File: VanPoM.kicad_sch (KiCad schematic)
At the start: 153 parts, among them IC1 TLV70433DBVT, IC2 UCC27517DBVR, IC3 SN74LV4052APWR, J1 Conn_03x26_Row_Letter_First, J10 UART3, J11 UART4, J2 OSTT7020150, J3 OSTT7020150, J4 OSTT7020150, J5 OSTT7020150, J6 OSTT7020150, J7 UART1, J8 UART1, J9 UART2, Q1 CSD18540Q5B, Q10 CSD18540Q5B, Q11 CSD18540Q5B, Q2 NX7002AK,215, Q3 BSS84W-7-F, Q4 CSD19531Q5A, Q5 CSD19531Q5A, Q6 CSD19531Q5A, Q7 CSD19531Q5A, Q8 CSD18540Q5B, Q9 CSD18540Q5B, U1 BQ34Z100-R2, U10 LM5009MM, U11 ESP32-S3-DEVKITC-1-N8R2, U12 TLA2528IRTER, U13 TVS3300DRV, U14 TVS3300DRV, U15 TVS3300DRV, U16 TVS3300DRV, U17 TVS3300DRV, U2 LM5109BMA/NOPB, U3 LM5109BMA/NOPB, U4 INA240A2D, U5 INA240A2D, U6 INA240A2D, U7 LM74700, U8 LM74700, U9 LM74700

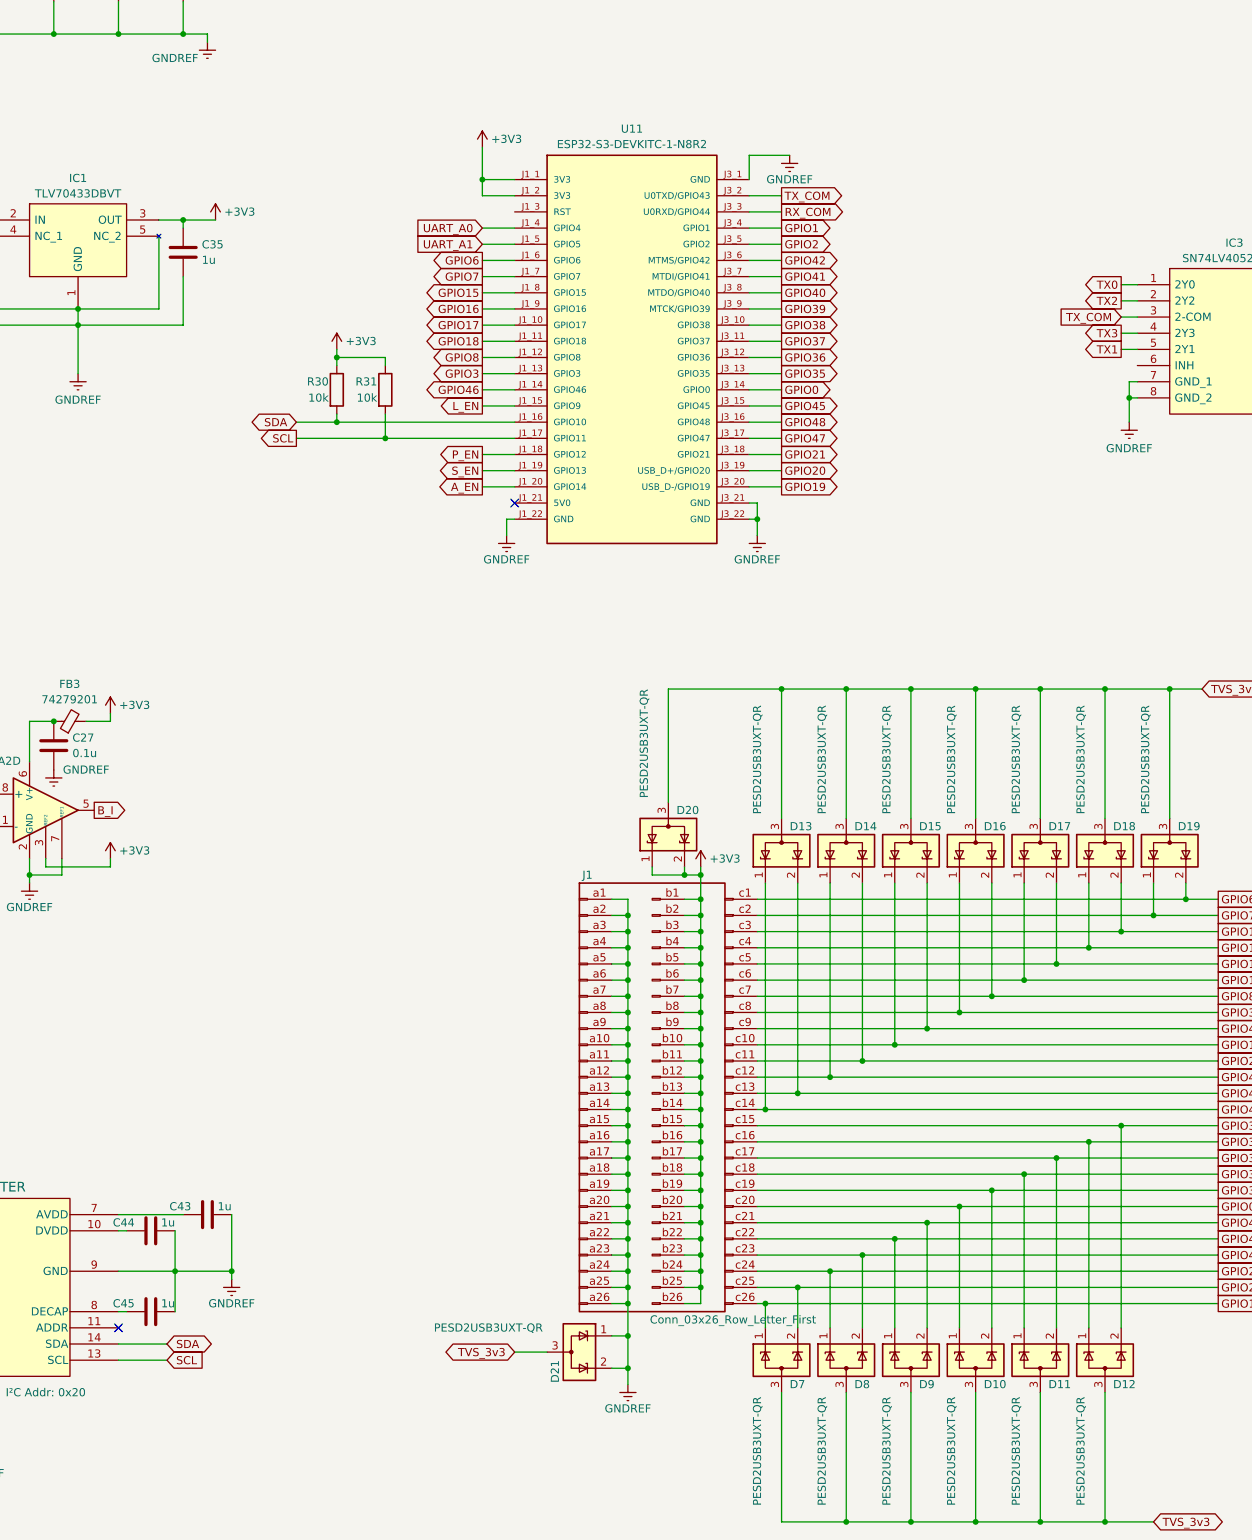
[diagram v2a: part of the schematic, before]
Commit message: + UART pull-ups
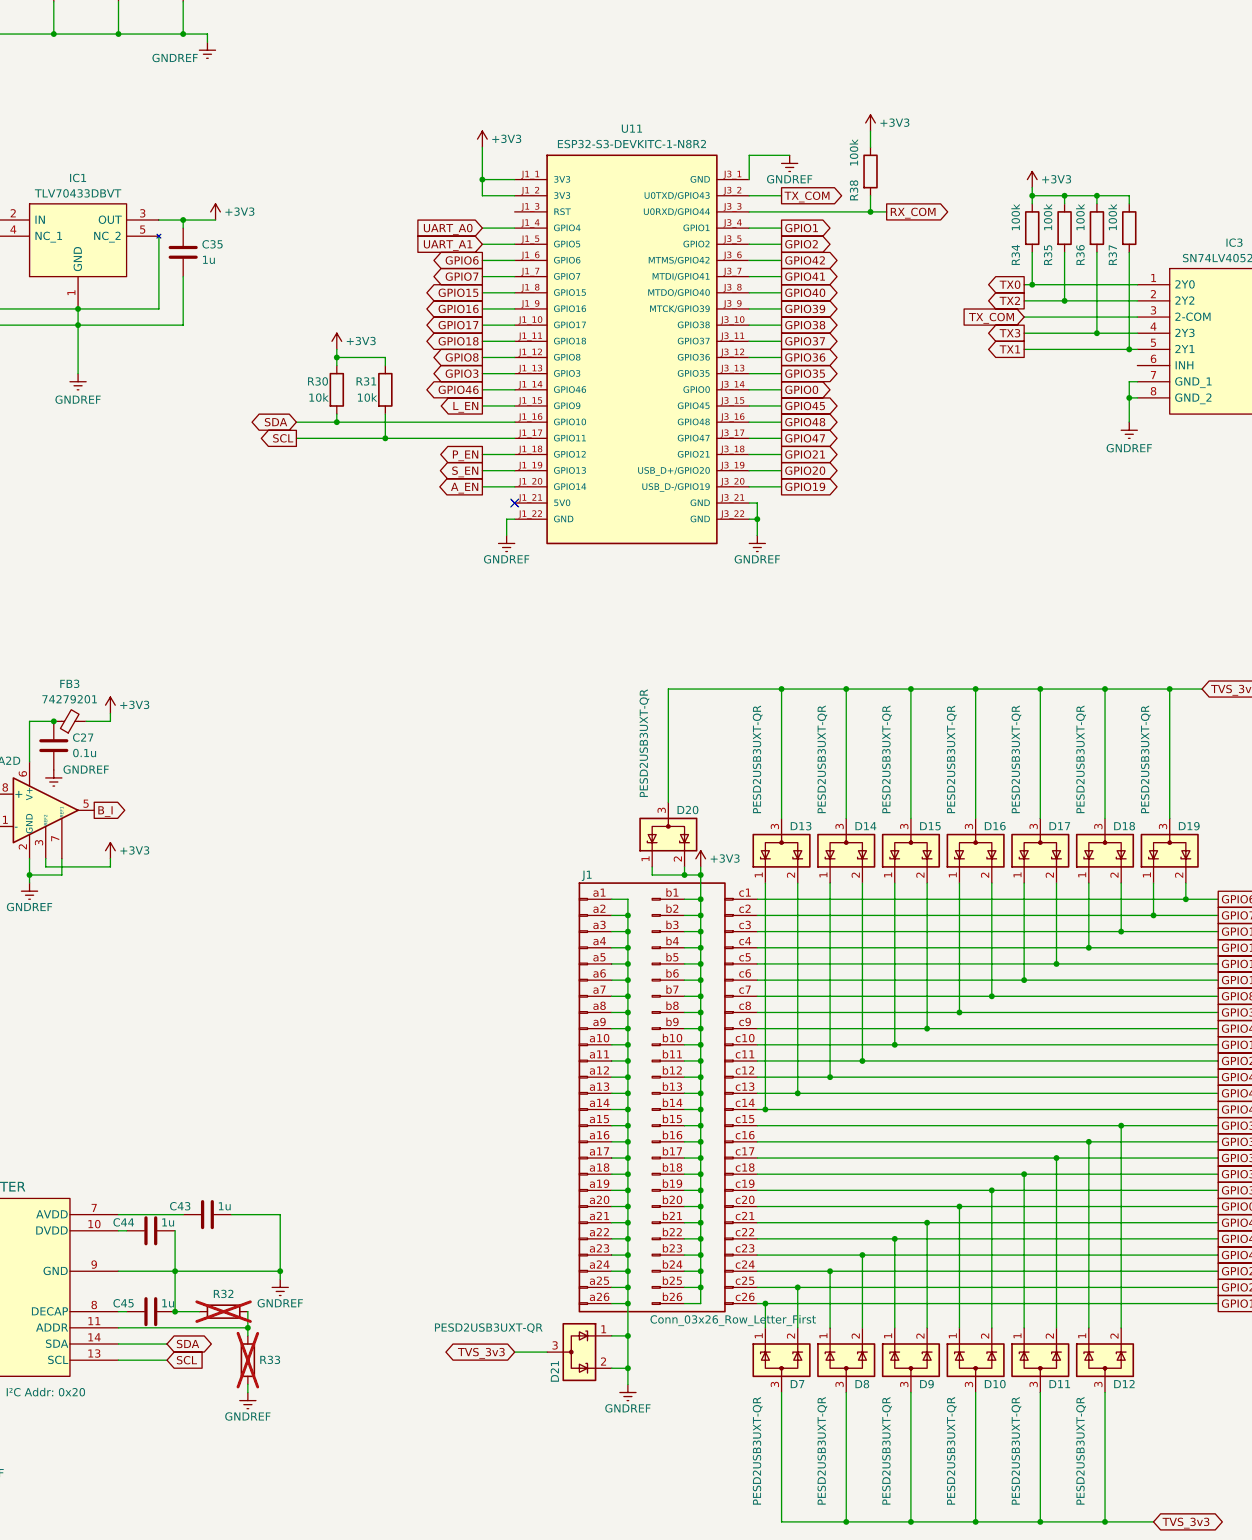
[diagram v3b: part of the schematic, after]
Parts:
- added R32, R33: R, symbol Device:R
- added R34, R35, R36, R37, R38: 100k, symbol Device:R
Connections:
- net +3V3: now also R34.1, R35.1, R36.1, R37.1, R38.1
- net GNDREF: now also R32.1, R33.1
- net RX_COM: now also R38.2
- net TX0: now also R34.2
- net TX1: now also R37.2
- net TX2: now also R35.2
- net TX3: now also R36.2
- net at U12.11 (ADDR): now also R32.2, R33.2
- no-connect marks 2 -> 1

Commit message: +++ PCB; f many small things
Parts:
- removed C30: 10u, symbol Perso:Cv
- removed C31: 1u, symbol Perso:Cv
- removed C32: 0.022u, symbol Perso:Cv
- removed C33: 10n, symbol Device:C
- removed D15, D16, D21: PESD2USB3UXT-QR, Package_TO_SOT_SMD:SOT-23, symbol Perso:PESD2USB3UXT-QR
- removed D6: B1100B-13-F, symbol Device:D_Schottky
- removed J1: Conn_03x26_Row_Letter_First, Perso:PinHeader_3x25_P2.54mm_Vertical, symbol Perso:Conn_03x26_Row_Letter_First
- removed J3: OSTT7020150, Perso:CONN2_OSTT7020150_OST, symbol Perso:OSTT7020150
- removed R21: 3.00, symbol Device:R
- removed R22, R23: 1.8M, symbol Device:R
- removed U10: LM5009MM, Package_SO:MSOP-8_3x3mm_P0.65mm, symbol Regulator_Switching:LM5009MM
- added C27: 10u, Capacitor_SMD:C_1210_3225Metric_Pad1.33x2.70mm_HandSolder, symbol Perso:Cv
- added C28: 0.022u, Capacitor_SMD:C_1206_3216Metric_Pad1.33x1.80mm_HandSolder, symbol Perso:Cv
- added C29: 50n, Capacitor_SMD:C_0402_1005Metric_Pad0.74x0.62mm_HandSolder, symbol Device:C
- added C30: 10n, Capacitor_SMD:C_0402_1005Metric_Pad0.74x0.62mm_HandSolder, symbol Device:C
- added C43: 0.1u, Capacitor_SMD:C_0603_1608Metric_Pad1.08x0.95mm_HandSolder, symbol Device:C
- added D6: PESD2USB3UXT-QR, Package_TO_SOT_SMD:SOT-23-3, symbol Perso:PESD2USB3UXT-QR
- added J5: OSTT7020150, TerminalBlock_MetzConnect:TerminalBlock_MetzConnect_Type073_RT02602HBLU_1x02_P5.08mm_Horizontal, symbol Perso:OSTT7020150
- added J6: Conn_03x23_Row_Letter_First, Perso:PinHeader_3x23_P2.54mm_Vertical, symbol Perso:Conn_03x23_Row_Letter_First
- added R30, R31: 200k, Resistor_SMD:R_0805_2012Metric_Pad1.20x1.40mm_HandSolder, symbol Device:R
- added U10: LM5163DDAR, Perso:SOIC-8-1EP_3.9x4.9mm_P1.27mm_EP2.34x2.34mm_ThermalVias, symbol Perso:LM5163DDAR
- added U18: TVS3300DRV, Package_SON:WSON-6-1EP_2x2mm_P0.65mm_EP1x1.6mm, symbol Perso:TVS3300DRV
- C1: renamed from C7; footprint (none) -> Capacitor_SMD:C_0603_1608Metric_Pad1.08x0.95mm_HandSolder; Manufacturer_Part_Number (none) -> GRM188R72A102KA01J; Price (none) -> 0.3
- C10: renamed from C8; footprint (none) -> Capacitor_SMD:C_0603_1608Metric_Pad1.08x0.95mm_HandSolder; Manufacturer_Part_Number (none) -> GRM188R72A102KA01J; Price (none) -> 0.3
- C11: renamed from C21; footprint (none) -> Capacitor_SMD:C_1210_3225Metric_Pad1.33x2.70mm_HandSolder; Manufacturer_Part_Number (none) -> GRM32EC72A106KE05K; Price (none) -> 0.83
- C12: renamed from C22; footprint (none) -> Capacitor_SMD:C_1210_3225Metric_Pad1.33x2.70mm_HandSolder; Manufacturer_Part_Number (none) -> GRM32EC72A106KE05K; Price (none) -> 0.83
- C13: renamed from C23; footprint (none) -> Capacitor_THT:CP_Radial_D16.0mm_P7.50mm; Manufacturer_Part_Number (none) -> EKYB800ELL102MLP1S; Price (none) -> 1.50
- C14: renamed from C1; footprint (none) -> Capacitor_SMD:C_0603_1608Metric_Pad1.08x0.95mm_HandSolder; Manufacturer_Part_Number (none) -> KGM15BR71H104JT; Price (none) -> 0.09
- C15: renamed from C2; value 1 -> 1u; footprint (none) -> Capacitor_SMD:C_0402_1005Metric_Pad0.74x0.62mm_HandSolder; Manufacturer_Part_Number (none) -> GRM155C81A105KA12D; Price (none) -> 0.09
- C16: renamed from C24; footprint (none) -> Capacitor_SMD:C_0603_1608Metric_Pad1.08x0.95mm_HandSolder; Manufacturer_Part_Number (none) -> KGM15BR71H104JT; Price (none) -> 0.09
- C17: renamed from C20; value 47u -> 0.1u; footprint (none) -> Capacitor_SMD:C_0603_1608Metric_Pad1.08x0.95mm_HandSolder; Manufacturer_Part_Number (none) -> KGM15BR71H104JT; Price (none) -> 0.09
- C18: renamed from C28; value 47u -> 0.1u; footprint (none) -> Capacitor_SMD:C_0603_1608Metric_Pad1.08x0.95mm_HandSolder; Manufacturer_Part_Number (none) -> KGM15BR71H104JT; Price (none) -> 0.09
- C19: renamed from C14; footprint (none) -> Capacitor_THT:CP_Radial_D18.0mm_P7.50mm; Manufacturer_Part_Number (none) -> EKY-800ELL122MM40S; Price (none) -> 1.83
- C2: renamed from C3; footprint (none) -> Capacitor_SMD:C_0805_2012Metric_Pad1.18x1.45mm_HandSolder; Manufacturer_Part_Number (none) -> KGM21AR71E105JU; Price (none) -> 0.3
- C20: renamed from C15; footprint (none) -> Capacitor_THT:CP_Radial_D18.0mm_P7.50mm; Manufacturer_Part_Number (none) -> EKY-800ELL122MM40S; Price (none) -> 1.83
- C21: renamed from C29; value 47u -> 0.1u; footprint (none) -> Capacitor_SMD:C_0603_1608Metric_Pad1.08x0.95mm_HandSolder; Manufacturer_Part_Number (none) -> KGM15BR71H104JT; Price (none) -> 0.09
- C22: renamed from C13; footprint (none) -> Capacitor_SMD:C_1206_3216Metric_Pad1.33x1.80mm_HandSolder; Manufacturer_Part_Number (none) -> GRM31CC72A475KE11L; Price (none) -> 0.6
- C23: renamed from C16; footprint (none) -> Capacitor_SMD:C_1206_3216Metric_Pad1.33x1.80mm_HandSolder; Manufacturer_Part_Number (none) -> GRM31CC72A475KE11L; Price (none) -> 0.6
- C24: renamed from C17; footprint (none) -> Capacitor_SMD:C_1206_3216Metric_Pad1.33x1.80mm_HandSolder; Manufacturer_Part_Number (none) -> GRM31CC72A475KE11L; Price (none) -> 0.6
- C25: renamed from C18; footprint (none) -> Capacitor_SMD:C_1206_3216Metric_Pad1.33x1.80mm_HandSolder; Manufacturer_Part_Number (none) -> GRM31CC72A475KE11L; Price (none) -> 0.6
- C26: renamed from C19; footprint (none) -> Capacitor_SMD:C_1206_3216Metric_Pad1.33x1.80mm_HandSolder; Manufacturer_Part_Number (none) -> GRM31CC72A475KE11L; Price (none) -> 0.6
- C3: renamed from C4; footprint (none) -> Capacitor_SMD:C_0603_1608Metric_Pad1.08x0.95mm_HandSolder; Manufacturer_Part_Number (none) -> 885012206004; Price (none) -> 0.05
- C31: renamed from C34; footprint (none) -> Capacitor_SMD:C_0805_2012Metric_Pad1.18x1.45mm_HandSolder; Manufacturer_Part_Number (none) -> KGM21AR71E105JU; Price (none) -> 0.3; Voltage (none) -> 25V
- C32: renamed from C35; footprint (none) -> Capacitor_SMD:C_0402_1005Metric_Pad0.74x0.62mm_HandSolder; Manufacturer_Part_Number (none) -> GRM155C81A105KA12D; Price (none) -> 0.09
- C33: renamed from C25; footprint (none) -> Capacitor_SMD:C_0603_1608Metric_Pad1.08x0.95mm_HandSolder; Manufacturer_Part_Number (none) -> KGM15BR71H104JT; Price (none) -> 0.09
- C34: renamed from C26; footprint (none) -> Capacitor_SMD:C_0603_1608Metric_Pad1.08x0.95mm_HandSolder; Manufacturer_Part_Number (none) -> KGM15BR71H104JT; Price (none) -> 0.09
- C35: renamed from C27; footprint (none) -> Capacitor_SMD:C_0603_1608Metric_Pad1.08x0.95mm_HandSolder; Manufacturer_Part_Number (none) -> KGM15BR71H104JT; Price (none) -> 0.09
- C36, C37, C38, C39, C40, C41, C42: footprint (none) -> Capacitor_SMD:C_0603_1608Metric_Pad1.08x0.95mm_HandSolder; Manufacturer_Part_Number (none) -> KGM15BR71H104JT; Price (none) -> 0.09
- C4: renamed from C5; footprint (none) -> Capacitor_SMD:C_0402_1005Metric_Pad0.74x0.62mm_HandSolder; Manufacturer_Part_Number (none) -> UMK105B7561KV-F; Price (none) -> 0.09
- C44, C45: footprint (none) -> Capacitor_SMD:C_0402_1005Metric_Pad0.74x0.62mm_HandSolder; Manufacturer_Part_Number (none) -> GRM155C81A105KA12D; Price (none) -> 0.09
- C46: renamed from C43; footprint (none) -> Capacitor_SMD:C_0402_1005Metric_Pad0.74x0.62mm_HandSolder; Manufacturer_Part_Number (none) -> GRM155C81A105KA12D; Price (none) -> 0.09
- C5: renamed from C6; footprint (none) -> Capacitor_SMD:C_0603_1608Metric_Pad1.08x0.95mm_HandSolder; Manufacturer_Part_Number (none) -> KGM15BR71H104JT; Price (none) -> 0.09
- C6: renamed from C12; footprint (none) -> Capacitor_SMD:C_0603_1608Metric_Pad1.08x0.95mm_HandSolder; Manufacturer_Part_Number (none) -> KGM15BR71H104JT; Price (none) -> 0.09
- C7: renamed from C11; footprint (none) -> Capacitor_SMD:C_0402_1005Metric_Pad0.74x0.62mm_HandSolder; Manufacturer_Part_Number (none) -> UMK105B7561KV-F; Price (none) -> 0.09
- C8: renamed from C10; footprint (none) -> Capacitor_SMD:C_0603_1608Metric_Pad1.08x0.95mm_HandSolder; Manufacturer_Part_Number (none) -> 885012206004; Price (none) -> 0.05
- C9: footprint (none) -> Capacitor_SMD:C_0805_2012Metric_Pad1.18x1.45mm_HandSolder; Manufacturer_Part_Number (none) -> KGM21AR71E105JU; Price (none) -> 0.3
- D1: renamed from D3; footprint (none) -> Diode_SMD:D_SMA; Manufacturer_Part_Number (none) -> B1100-13-F; Price (none) -> 0.28
- D10: renamed from D8; footprint Package_TO_SOT_SMD:SOT-23 -> Package_TO_SOT_SMD:SOT-23-3; Manufacturer_Part_Number (none) -> PESD2USB3UXT-QR; Price (none) -> 0.25
- D11: renamed from D14; footprint Package_TO_SOT_SMD:SOT-23 -> Package_TO_SOT_SMD:SOT-23-3; Manufacturer_Part_Number (none) -> PESD2USB3UXT-QR; Price (none) -> 0.25
- D12: renamed from D9; footprint Package_TO_SOT_SMD:SOT-23 -> Package_TO_SOT_SMD:SOT-23-3; Manufacturer_Part_Number (none) -> PESD2USB3UXT-QR; Price (none) -> 0.25
- D13: renamed from D17; footprint Package_TO_SOT_SMD:SOT-23 -> Package_TO_SOT_SMD:SOT-23-3; Manufacturer_Part_Number (none) -> PESD2USB3UXT-QR; Price (none) -> 0.25
- D14: renamed from D10; footprint Package_TO_SOT_SMD:SOT-23 -> Package_TO_SOT_SMD:SOT-23-3; Manufacturer_Part_Number (none) -> PESD2USB3UXT-QR; Price (none) -> 0.25
- D15: renamed from D18; footprint Package_TO_SOT_SMD:SOT-23 -> Package_TO_SOT_SMD:SOT-23-3; Manufacturer_Part_Number (none) -> PESD2USB3UXT-QR; Price (none) -> 0.25
- D16: renamed from D11; footprint Package_TO_SOT_SMD:SOT-23 -> Package_TO_SOT_SMD:SOT-23-3; Manufacturer_Part_Number (none) -> PESD2USB3UXT-QR; Price (none) -> 0.25
- D17: renamed from D19; footprint Package_TO_SOT_SMD:SOT-23 -> Package_TO_SOT_SMD:SOT-23-3; Manufacturer_Part_Number (none) -> PESD2USB3UXT-QR; Price (none) -> 0.25
- D18: renamed from D12; footprint Package_TO_SOT_SMD:SOT-23 -> Package_TO_SOT_SMD:SOT-23-3; Manufacturer_Part_Number (none) -> PESD2USB3UXT-QR; Price (none) -> 0.25
- D2: footprint (none) -> Diode_SMD:D_SMA; Manufacturer_Part_Number (none) -> MURA110T3G; Price (none) -> 0.46
- D21: renamed from D25; footprint Package_TO_SOT_SMD:SOT-23 -> Package_TO_SOT_SMD:SOT-23-3; Manufacturer_Part_Number (none) -> PESD2USB3UXT-QR; Price (none) -> 0.25
- D22: renamed from D24; footprint Package_TO_SOT_SMD:SOT-23 -> Package_TO_SOT_SMD:SOT-23-3; Manufacturer_Part_Number (none) -> PESD2USB3UXT-QR; Price (none) -> 0.25
- D23: footprint Package_TO_SOT_SMD:SOT-23 -> Package_TO_SOT_SMD:SOT-23-3; Manufacturer_Part_Number (none) -> PESD2USB3UXT-QR; Price (none) -> 0.25
- D24: renamed from D22; footprint Package_TO_SOT_SMD:SOT-23 -> Package_TO_SOT_SMD:SOT-23-3; Manufacturer_Part_Number (none) -> PESD2USB3UXT-QR; Price (none) -> 0.25
- D25: renamed from D26; footprint Package_TO_SOT_SMD:SOT-23 -> Package_TO_SOT_SMD:SOT-23-3; Manufacturer_Part_Number (none) -> PESD2USB3UXT-QR; Price (none) -> 0.25
- D3: renamed from D5; footprint (none) -> Diode_SMD:D_SMA; Manufacturer_Part_Number (none) -> MURA110T3G; Price (none) -> 0.46
- D4: footprint (none) -> Diode_SMD:D_SMA; Manufacturer_Part_Number (none) -> B1100-13-F; Price (none) -> 0.28
- D5: renamed from D1; footprint (none) -> Diode_SMD:D_SOD-123; Manufacturer_Part_Number (none) -> BZT52C15-7-F; Price (none) -> 0.13
- D7: renamed from D20; footprint Package_TO_SOT_SMD:SOT-23 -> Package_TO_SOT_SMD:SOT-23-3; Manufacturer_Part_Number (none) -> PESD2USB3UXT-QR; Price (none) -> 0.25
- D8: renamed from D7; footprint Package_TO_SOT_SMD:SOT-23 -> Package_TO_SOT_SMD:SOT-23-3; Manufacturer_Part_Number (none) -> PESD2USB3UXT-QR; Price (none) -> 0.25
- D9: renamed from D13; footprint Package_TO_SOT_SMD:SOT-23 -> Package_TO_SOT_SMD:SOT-23-3; Manufacturer_Part_Number (none) -> PESD2USB3UXT-QR; Price (none) -> 0.25
- FB1, FB2, FB3: footprint (none) -> Capacitor_SMD:C_0805_2012Metric_Pad1.18x1.45mm_HandSolder; Manufacturer_Part_Number (none) -> 74279201; Price (none) -> 0.20
- IC1: renamed from IC2; Price (none) -> 0.78
- IC2: renamed from IC1; Price (none) -> 0.78
- IC3: Price (none) -> 0.39
- J1: renamed from J5; footprint Perso:CONN2_OSTT7020150_OST -> TerminalBlock_MetzConnect:TerminalBlock_MetzConnect_Type073_RT02602HBLU_1x02_P5.08mm_Horizontal; Manufacturer_Part_Number (none) -> EM290802; Price (none) -> 1.58
- J10: renamed from J8; footprint (none) -> Connector_PinHeader_2.54mm:PinHeader_1x04_P2.54mm_Vertical; Manufacturer_Part_Number (none) -> G800W304018EU; Price (none) -> 0.10
- J11: renamed from J7; value UART1 -> I2C; footprint (none) -> Connector_PinHeader_2.54mm:PinHeader_1x04_P2.54mm_Vertical; Manufacturer_Part_Number (none) -> G800W304018EU; Price (none) -> 0.10
- J2, J4: footprint Perso:CONN2_OSTT7020150_OST -> TerminalBlock_MetzConnect:TerminalBlock_MetzConnect_Type073_RT02602HBLU_1x02_P5.08mm_Horizontal; Manufacturer_Part_Number (none) -> EM290802; Price (none) -> 1.58
- J3: renamed from J6; footprint Perso:CONN2_OSTT7020150_OST -> TerminalBlock_MetzConnect:TerminalBlock_MetzConnect_Type073_RT02602HBLU_1x02_P5.08mm_Horizontal; Manufacturer_Part_Number (none) -> EM290802; Price (none) -> 1.58
- J7: renamed from J11; footprint (none) -> Connector_PinHeader_2.54mm:PinHeader_1x04_P2.54mm_Vertical; Manufacturer_Part_Number (none) -> G800W304018EU; Price (none) -> 0.10
- J8: renamed from J10; footprint (none) -> Connector_PinHeader_2.54mm:PinHeader_1x04_P2.54mm_Vertical; Manufacturer_Part_Number (none) -> G800W304018EU; Price (none) -> 0.10
- J9: footprint (none) -> Connector_PinHeader_2.54mm:PinHeader_1x04_P2.54mm_Vertical; Manufacturer_Part_Number (none) -> G800W304018EU; Price (none) -> 0.10
- L1, L2: footprint (none) -> Inductor_SMD:L_Wuerth_HCF-2818; Manufacturer_Part_Number (none) -> 7443642200; Price (none) -> 9.27
- L3: footprint (none) -> Perso:INDPM105103X500N; Manufacturer_Part_Number (none) -> DR1050-221-R; Price (none) -> 0.94
- Q1: renamed from Q5; footprint Package_TO_SOT_SMD:TDSON-8-1 -> Package_SON:VSONP-8-1EP_5x6_P1.27mm; symbol Transistor_FET:CSD19531Q5A -> Perso:CSD19531Q5A; Manufacturer_Part_Number (none) -> CSD19531Q5A; Price (none) -> 1.58
- Q10, Q11: footprint Package_TO_SOT_SMD:TDSON-8-1 -> Package_SON:VSONP-8-1EP_5x6_P1.27mm; symbol Transistor_FET:CSD18540Q5B -> Perso:CSD18540Q5B; Manufacturer_Part_Number (none) -> CSD18540Q5B; Price (none) -> 2.25
- Q2: renamed from Q4; footprint Package_TO_SOT_SMD:TDSON-8-1 -> Package_SON:VSONP-8-1EP_5x6_P1.27mm; symbol Transistor_FET:CSD19531Q5A -> Perso:CSD19531Q5A; Manufacturer_Part_Number (none) -> CSD19531Q5A; Price (none) -> 1.58
- Q3: renamed from Q7; footprint Package_TO_SOT_SMD:TDSON-8-1 -> Package_SON:VSONP-8-1EP_5x6_P1.27mm; symbol Transistor_FET:CSD19531Q5A -> Perso:CSD19531Q5A; Manufacturer_Part_Number (none) -> CSD19531Q5A; Price (none) -> 1.58
- Q4: renamed from Q6; footprint Package_TO_SOT_SMD:TDSON-8-1 -> Package_SON:VSONP-8-1EP_5x6_P1.27mm; symbol Transistor_FET:CSD19531Q5A -> Perso:CSD19531Q5A; Manufacturer_Part_Number (none) -> CSD19531Q5A; Price (none) -> 1.58
- Q5: renamed from Q2; footprint Package_TO_SOT_THT:TO-220-3_Vertical -> Package_TO_SOT_SMD:SOT-23-3; Manufacturer_Part_Number (none) -> NX7002AK,215; Price (none) -> 0.13
- Q6: renamed from Q3; footprint Package_TO_SOT_THT:TO-220-3_Vertical -> Package_TO_SOT_SMD:SOT-323_SC-70_Handsoldering; symbol Perso:IPP120P04P4L03AKSA2 -> Transistor_FET:BSS84; Manufacturer_Part_Number (none) -> BSS84W-7-F; Price (none) -> 0.35
- Q7: renamed from Q9; footprint Package_TO_SOT_SMD:TDSON-8-1 -> Package_SON:VSONP-8-1EP_5x6_P1.27mm; symbol Transistor_FET:CSD18540Q5B -> Perso:CSD18540Q5B; Manufacturer_Part_Number (none) -> CSD18540Q5B; Price (none) -> 2.25
- Q8: renamed from Q1; footprint Package_TO_SOT_SMD:TDSON-8-1 -> Package_SON:VSONP-8-1EP_5x6_P1.27mm; symbol Transistor_FET:CSD18540Q5B -> Perso:CSD18540Q5B; Manufacturer_Part_Number (none) -> CSD18540Q5B; Price (none) -> 2.25
- Q9: renamed from Q8; footprint Package_TO_SOT_SMD:TDSON-8-1 -> Package_SON:VSONP-8-1EP_5x6_P1.27mm; symbol Transistor_FET:CSD18540Q5B -> Perso:CSD18540Q5B; Manufacturer_Part_Number (none) -> CSD18540Q5B; Price (none) -> 2.25
- R1: renamed from R9; footprint (none) -> Resistor_SMD:R_0805_2012Metric_Pad1.20x1.40mm_HandSolder; Manufacturer_Part_Number (none) -> RK73H2ATTD5R60F; Price (none) -> 0.02
- R10: renamed from R3; footprint (none) -> Resistor_SMD:R_0805_2012Metric_Pad1.20x1.40mm_HandSolder; Manufacturer_Part_Number (none) -> CRG0805F330K; Price (none) -> 0.09
- R11: renamed from R4; footprint (none) -> Resistor_SMD:R_0805_2012Metric_Pad1.20x1.40mm_HandSolder; Manufacturer_Part_Number (none) -> RC0805FR-10390KL; Price (none) -> 0.09
- R12: renamed from R5; footprint (none) -> Resistor_SMD:R_0805_2012Metric_Pad1.20x1.40mm_HandSolder; Manufacturer_Part_Number (none) -> RK73H2ATTD3002F; Price (none) -> 0.02
- R13: renamed from R15; footprint (none) -> Resistor_SMD:R_0805_2012Metric_Pad1.20x1.40mm_HandSolder; Manufacturer_Part_Number (none) -> AC0805FR-7W10KL; Price (none) -> 0.02
- R14: renamed from R1; footprint (none) -> Resistor_SMD:R_0805_2012Metric_Pad1.20x1.40mm_HandSolder; Manufacturer_Part_Number (none) -> RK73H2ATTD5R11F; Price (none) -> 0.10
- R15: renamed from R16; footprint (none) -> Resistor_SMD:R_0805_2012Metric_Pad1.20x1.40mm_HandSolder; Manufacturer_Part_Number (none) -> RK73H2ATTD1003F; Price (none) -> 0.02
- R16: renamed from R14; footprint (none) -> Resistor_SMD:R_0805_2012Metric_Pad1.20x1.40mm_HandSolder; Manufacturer_Part_Number (none) -> RK73H2ATTD1003F; Price (none) -> 0.02
- R17: value 430k -> 140k; footprint (none) -> Resistor_SMD:R_0805_2012Metric_Pad1.20x1.40mm_HandSolder; Manufacturer_Part_Number (none) -> RK73H2ATTD1400F; Price (none) -> 0.02
- R18: value 169k -> 220k; footprint (none) -> Resistor_SMD:R_0805_2012Metric_Pad1.20x1.40mm_HandSolder; Manufacturer_Part_Number (none) -> RK73H2ATTDD2203F; Price (none) -> 0.03
- R19: value 3.00k -> 30k; footprint (none) -> Resistor_SMD:R_0805_2012Metric_Pad1.20x1.40mm_HandSolder; Manufacturer_Part_Number (none) -> RK73H2ATTD3002F; Price (none) -> 0.02
- R2: renamed from R8; footprint (none) -> Resistor_SMD:R_0805_2012Metric_Pad1.20x1.40mm_HandSolder; Manufacturer_Part_Number (none) -> RK73H2ATTD4R42F; Price (none) -> 0.02
- R20: value 1.00k -> 3.00; footprint (none) -> Resistor_SMD:R_0805_2012Metric_Pad1.20x1.40mm_HandSolder; Manufacturer_Part_Number (none) -> RK73H2ATTD3R00F; Price (none) -> 0.02
- R21: renamed from R30; footprint (none) -> Resistor_SMD:R_0805_2012Metric_Pad1.20x1.40mm_HandSolder; Manufacturer_Part_Number (none) -> AC0805FR-7W10KL; Price (none) -> 0.02
- R22: renamed from R31; footprint (none) -> Resistor_SMD:R_0805_2012Metric_Pad1.20x1.40mm_HandSolder; Manufacturer_Part_Number (none) -> AC0805FR-7W10KL; Price (none) -> 0.02
- R23: renamed from R38; footprint (none) -> Resistor_SMD:R_0805_2012Metric_Pad1.20x1.40mm_HandSolder; Manufacturer_Part_Number (none) -> RK73H2ATTD1003F; Price (none) -> 0.02
- R24, R25: footprint (none) -> Resistor_SMD:R_0805_2012Metric_Pad1.20x1.40mm_HandSolder; Manufacturer_Part_Number (none) -> RK73H2ATTD1804F; Price (none) -> 0.02
- R26, R27: value 200k -> 1.8M; footprint (none) -> Resistor_SMD:R_0805_2012Metric_Pad1.20x1.40mm_HandSolder; Manufacturer_Part_Number (none) -> RK73H2ATTD1804F; Price (none) -> 0.02
- R28, R29: footprint (none) -> Resistor_SMD:R_0805_2012Metric_Pad1.20x1.40mm_HandSolder; Manufacturer_Part_Number (none) -> RK73H2ATTDD2003F; Price (none) -> 0.03
- R3: renamed from R7; footprint (none) -> Resistor_SMD:R_0805_2012Metric_Pad1.20x1.40mm_HandSolder; Manufacturer_Part_Number (none) -> RK73H2ATTD2R21F; Price (none) -> 0.02
- R32, R33: footprint (none) -> Resistor_SMD:R_0805_2012Metric_Pad1.20x1.40mm_HandSolder
- R34, R35, R36, R37: footprint (none) -> Resistor_SMD:R_0805_2012Metric_Pad1.20x1.40mm_HandSolder; Manufacturer_Part_Number (none) -> RK73H2ATTD1003F; Price (none) -> 0.02
- R4: renamed from R6; footprint (none) -> Resistor_SMD:R_0805_2012Metric_Pad1.20x1.40mm_HandSolder; Manufacturer_Part_Number (none) -> RK73H2ATTD2R21F; Price (none) -> 0.02
- R5: renamed from R13; footprint (none) -> Resistor_SMD:R_0805_2012Metric_Pad1.20x1.40mm_HandSolder; Manufacturer_Part_Number (none) -> RK73H2ATTD2R21F; Price (none) -> 0.02
- R6: renamed from R12; footprint (none) -> Resistor_SMD:R_0805_2012Metric_Pad1.20x1.40mm_HandSolder; Manufacturer_Part_Number (none) -> RK73H2ATTD2R21F; Price (none) -> 0.02
- R7: renamed from R11; footprint (none) -> Resistor_SMD:R_0805_2012Metric_Pad1.20x1.40mm_HandSolder; Manufacturer_Part_Number (none) -> RK73H2ATTD4R42F; Price (none) -> 0.02
- R8: renamed from R10; footprint (none) -> Resistor_SMD:R_0805_2012Metric_Pad1.20x1.40mm_HandSolder; Manufacturer_Part_Number (none) -> RK73H2ATTD5R60F; Price (none) -> 0.02
- R9: renamed from R2; footprint (none) -> Resistor_SMD:R_0805_2012Metric_Pad1.20x1.40mm_HandSolder; Manufacturer_Part_Number (none) -> RC0805FR-07240KL; Price (none) -> 0.09
- R_sense1: renamed from R_sense3; footprint (none) -> Perso:R_Shunt_Ohmite_LVK25-fixed; symbol Device:R -> Device:R_Shunt; Manufacturer_Part_Number (none) -> LVK25R002DER; Price (none) -> 1.66
- R_sense2: renamed from R_sense1; footprint (none) -> Perso:R_Shunt_Ohmite_LVK25-fixed; symbol Device:R -> Device:R_Shunt; Manufacturer_Part_Number (none) -> LVK25R002DER; Price (none) -> 1.66
- R_sense3: renamed from R_sense2; footprint (none) -> Perso:R_Shunt_Ohmite_LVK25-fixed; symbol Device:R -> Device:R_Shunt; Manufacturer_Part_Number (none) -> LVK25R002DER; Price (none) -> 1.66
- U1: renamed from U2; Manufacturer_Part_Number (none) -> LM5109BMA/NOPB; Price (none) -> 0.87
- U11: renamed from U16; Manufacturer_Part_Number (none) -> TVS3300DRVR; Price (none) -> 0.61
- U12: renamed from U17; Manufacturer_Part_Number (none) -> TVS3300DRVR; Price (none) -> 0.61
- U13: renamed from U11; value ESP32-S3-DEVKITC-1-N8R2 -> ESP32-S3-DEVKITC-1-N16R2; footprint ESP32-S3-DEVKITC-1-N8R2:XCVR_ESP32-S3-DEVKITC-1-N8R2 -> Perso:XCVR_ESP32-S3-DEVKITC-1
- U14: renamed from U4; Manufacturer_Part_Number (none) -> INA240A2D; Price (none) -> 3.61
- U15: renamed from U5; Manufacturer_Part_Number (none) -> INA240A2D; Price (none) -> 3.61
- U16: renamed from U6; Manufacturer_Part_Number (none) -> INA240A2D; Price (none) -> 3.61
- U17: renamed from U12; Manufacturer_Part_Number (none) -> TLA2528IRTER; Price (none) -> 4.11
- U2: renamed from U3; Manufacturer_Part_Number (none) -> LM5109BMA/NOPB; Price (none) -> 0.87
- U3: renamed from U1; Manufacturer_Part_Number (none) -> BQ34Z100-R2; Price (none) -> 4.26
- U4: renamed from U14; Manufacturer_Part_Number (none) -> TVS3300DRVR; Price (none) -> 0.61
- U5: renamed from U13; Manufacturer_Part_Number (none) -> TVS3300DRVR; Price (none) -> 0.61
- U6: renamed from U8; Manufacturer_Part_Number (none) -> LM74700QDBVTQ1; Price (none) -> 2.12
- U7: Manufacturer_Part_Number (none) -> LM74700QDBVTQ1; Price (none) -> 2.12
- U8: renamed from U9; Manufacturer_Part_Number (none) -> LM74700QDBVTQ1; Price (none) -> 2.12
- U9: renamed from U15; Manufacturer_Part_Number (none) -> TVS3300DRVR; Price (none) -> 0.61
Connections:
- net RX4 is gone; now on net RX3: D21.2 (K), J7.2 (Pin_2)
- net TX4 is gone; now on net TX3: D21.1 (K), J7.3 (Pin_3)
- net +10V: now also L3.2, R18.1, R20.1
- net +3V3: now also J6.b1 (Pin_b1), J6.b10 (Pin_b10), J6.b11 (Pin_b11), J6.b12 (Pin_b12), J6.b13 (Pin_b13), J6.b14 (Pin_b14), J6.b15 (Pin_b15), J6.b16 (Pin_b16), J6.b17 (Pin_b17), J6.b18 (Pin_b18), J6.b19 (Pin_b19), J6.b2 (Pin_b2), J6.b20 (Pin_b20), J6.b21 (Pin_b21), J6.b22 (Pin_b22), J6.b23 (Pin_b23), J6.b3 (Pin_b3), J6.b4 (Pin_b4), J6.b5 (Pin_b5), J6.b6 (Pin_b6), J6.b7 (Pin_b7), J6.b8 (Pin_b8), J6.b9 (Pin_b9); no longer D7.1 (K)
- net BAT+: now also J4.2 (Pin_2), Q6.2 (S), R27.1, R_sense1.1, J5.2 (Pin_2); no longer J4.1 (Pin_1), Q6.3 (S), R25.1, R_sense1.2, U15.1 (-)
- net BAT-: now also J4.1 (Pin_1), R_sense2.4; no longer R_sense2.1, U16.1 (-), U3.9 (SRP)
- net GNDREF: now also IC3.6 (INH), Q5.2 (S), R17.1, R19.2, C27.1, C30.2, C43.2, D6.1 (K), D6.2 (K), J6.c1 (Pin_c1), J6.c10 (Pin_c10), J6.c11 (Pin_c11), J6.c12 (Pin_c12), J6.c13 (Pin_c13), J6.c14 (Pin_c14), J6.c15 (Pin_c15), J6.c16 (Pin_c16), J6.c17 (Pin_c17), J6.c18 (Pin_c18), J6.c19 (Pin_c19), J6.c2 (Pin_c2), J6.c20 (Pin_c20), J6.c21 (Pin_c21), J6.c22 (Pin_c22), J6.c23 (Pin_c23), J6.c3 (Pin_c3), J6.c4 (Pin_c4), J6.c5 (Pin_c5), J6.c6 (Pin_c6), J6.c7 (Pin_b7), J6.c8 (Pin_b8), J6.c9 (Pin_c9), R30.2, R31.2, U10.1 (GND); no longer Q1.2 (S), Q1.3 (S), Q4.2 (S), Q4.3 (S), Q5.1 (G), Q7.2 (S), Q7.3 (S), Q8.2 (S), Q8.3 (S), R18.1, R20.2, R26.2, R27.2, R32.1
- net GPIO0: now also D13.1 (K), J6.a7 (Pin_a7); no longer D14.1 (K)
- net GPIO1: now also D18.1 (K), J6.a13 (Pin_a13)
- net GPIO15: now also D10.2 (K), J6.a20 (Pin_a20); no longer D15.2 (K)
- net GPIO16: now also D12.1 (K), J6.a19 (Pin_a19); no longer D15.1 (K)
- net GPIO17: now also D12.2 (K), J6.a18 (Pin_a18); no longer D13.2 (K)
- net GPIO18: now also D14.1 (K), J6.a17 (Pin_a17); no longer D13.1 (K)
- net GPIO19: now also D7.1 (K), J6.a1 (Pin_a1); no longer D8.1 (K)
- net GPIO2: now also D18.2 (K), J6.a12 (Pin_a12); no longer D11.2 (K)
- net GPIO20: now also D17.2 (K), J6.a2 (Pin_a2); no longer D8.2 (K)
- net GPIO21: now also D17.1 (K), J6.a3 (Pin_a3); no longer D10.1 (K)
- net GPIO3: now also D16.1 (K), J6.a15 (Pin_a15)
- net GPIO39: now also D11.2 (K), J6.a8 (Pin_a8); no longer D18.2 (K)
- net GPIO40: now also D11.1 (K), J6.a9 (Pin_a9); no longer D9.1 (K)
- net GPIO41: now also J6.a10 (Pin_a10)
- net GPIO42: now also D9.1 (K), J6.a11 (Pin_a11); no longer D11.1 (K)
- net GPIO45: now also D13.2 (K), J6.a6 (Pin_a6); no longer D12.2 (K)
- net GPIO46: now also D16.2 (K), J6.a14 (Pin_a14)
- net GPIO47: now also D15.2 (K), J6.a4 (Pin_a4); no longer D10.2 (K)
- net GPIO48: now also D15.1 (K), J6.a5 (Pin_a5); no longer D12.1 (K)
- net GPIO6: now also D8.2 (K), J6.a22 (Pin_a22); no longer D17.2 (K)
- net GPIO7: now also D10.1 (K), J6.a21 (Pin_a21); no longer D17.1 (K)
- net GPIO8: now also D14.2 (K), J6.a16 (Pin_a16)
- net OUT-: now also Q8.3 (D), J5.1 (Pin_1), U18.4 (IN), U18.5 (IN), U18.6 (IN); no longer J4.2 (Pin_2), Q8.5 (D)
- net P+: now also R_sense3.4; no longer R_sense3.1, U14.8 (+)
- net PW_H1: now also U13.J3_10 (GPIO38)
- net PW_H2: now also U13.J3_12 (GPIO36)
- net PW_L1: now also U13.J3_11 (GPIO37)
- net PW_L2: now also U13.J3_13 (GPIO35)
- net RX0: now also D24.2 (K), J10.2 (Pin_2)
- net RX1: now also D23.2 (K), J9.2 (Pin_2); no longer D24.2 (K), J10.2 (Pin_2)
- net RX2: now also D22.2 (K), J8.2 (Pin_2); no longer D23.2 (K), J9.2 (Pin_2)
- net RX3: no longer D22.2 (K), J8.2 (Pin_2)
- net TVS: now also U4.1 (GND), U4.2 (GND), U4.3 (GND), U4.7 (GND), U5.1 (GND), U5.2 (GND), U5.3 (GND), U5.7 (GND), U18.1 (GND), U18.2 (GND), U18.3 (GND), U18.7 (GND)
- net TVS_3v3: now also D6.3 (A)
- net TX0: now also D24.1 (K), J10.3 (Pin_3)
- net TX1: now also D23.1 (K), J9.3 (Pin_3); no longer D24.1 (K), J10.3 (Pin_3)
- net TX2: now also D22.1 (K), J8.3 (Pin_3); no longer D23.1 (K), J9.3 (Pin_3)
- net TX3: no longer D22.1 (K), J8.3 (Pin_3)
- net V_A: now also R25.1; no longer Q11.2 (S), Q11.3 (S)
- net V_IN: now also Q10.3 (D), Q11.3 (D), Q2.3 (D), Q3.3 (D), Q9.3 (D), C27.2, U10.2 (VIN), U10.3 (EN/UVLO); no longer Q10.5 (D), Q11.5 (D), Q2.5 (D), Q3.5 (D), Q9.5 (D), R17.1
- net V_S: now also R24.1; no longer Q9.2 (S), Q9.3 (S)
- net at R14.1: now also Q8.2 (G); no longer Q8.4 (G)
- net at R19.1: now also R18.2, C29.2, U10.5 (FB); no longer L3.2
- net at U6.5 (GATE): now also Q9.2 (G); no longer Q9.4 (G)
- net AIO_1: now reaches R28.1, U17.16 (AIN1/GPIO1)
- net AIO_1: now also C36.1, R27.2; no longer C38.1
- net AIO_7: now reaches U17.6 (AIN7/GPIO7)
- net AIO_7: now also C38.1, R25.2, R30.1
- net at C45.1, U17.8 (DECAP): now also R32.1
- net at D5.1 (K), R13.2: now also Q7.2 (G); no longer Q7.4 (G)
- net at R5.1: now also U2.7 (HO); no longer Q3.4 (G)
- net at R5.2: now also Q3.2 (G); no longer U2.7 (HO)
- net at R10.1, R9.2: now also Q6.1 (G); no longer Q6.2 (G)
- net at R4.1: now also U1.7 (HO); no longer Q2.4 (G)
- net at R4.2: now also Q2.2 (G); no longer U1.7 (HO)
- net at U7.5 (GATE): now also Q10.2 (G); no longer Q10.4 (G)
- net at C5.1, D1.1 (K), U1.6 (HS): now also R3.1; no longer R3.2
- net at C6.1, D4.1 (K), U2.6 (HS): now also R6.1; no longer R6.2
- net at L3.1: now also C28.1, C29.1, U10.8 (SW)
- net at R11.1: now also Q6.3 (D); no longer Q6.1 (D)
- net at U8.5 (GATE): now also Q11.2 (G); no longer Q11.4 (G)
- net at R2.2: now also Q1.2 (G); no longer Q1.4 (G)
- net at R17.2: now also U10.4 (RON)
- net at R10.2: now also Q5.3 (D); no longer Q5.2 (D)
- net at R7.2: now also Q4.2 (G); no longer Q4.4 (G)
- net ? renamed 103AT
- net 103AT: now also C40.1, D8.1 (K), U17.2 (AIN3/GPIO3), J6.a23 (Pin_a23)
- removed net B_I: C40.1, U16.5, U17.5 (AIN6/GPIO6)
- net B_S+ renamed B-_S+
- net B-_S+: no longer Q7.5 (D)
- removed net Bu_I: C41.1, U15.5, U17.4 (AIN5/GPIO5)
- net Bu_S: no longer names the net of C11.1, C12.1, C13.1, L1.1
- net Bu_S: now also L2.2, R_sense1.4; no longer L2.1, R_sense1.1, U15.8 (+)
- removed net GPIO35: D14.2 (K), U13.J3_13 (GPIO35)
- removed net GPIO36: D16.1 (K), U13.J3_12 (GPIO36)
- removed net GPIO37: D16.2 (K), U13.J3_11 (GPIO37)
- removed net GPIO38: D18.1 (K), U13.J3_10 (GPIO38)
- net P_I renamed AIO_4
- net AIO_4: now also C43.1; no longer C42.1
- removed net P_S-: C18.2, Q10.1 (S), Q10.2 (S), Q10.3 (S), R24.1, R_sense3.2, U14.1 (-), U7.6 (ANODE)
- new net: C30.1, R20.2
- new net: L2.1, Q3.1 (S), Q4.3 (D), R6.2, R8.1
- new net: L1.2, Q1.3 (D), Q2.1 (S), R1.1, R3.2
- new net: C28.2, U10.7 (BST)
- new net: Q7.3 (D), R_sense2.1
- new net AIO_0: C42.1, U15.5, U17.15 (AIN0/GPIO0)
- new net AIO_2: C41.1, U16.5, U17.1 (AIN2/GPIO2)
- new net AIO_5: C37.1, R26.2, R29.1, U17.4 (AIN5/GPIO5)
- new net AIO_6: C39.1, R24.2, R31.1, U17.5 (AIN6/GPIO6)
- new net B-_S-: R_sense2.3, U16.1 (-), U3.9 (SRP)
- new net Bu+_S+: R_sense1.3, U15.8 (+)
- new net Bu+_S-: R_sense1.2, U15.1 (-)
- new net P+_S+: R_sense3.3, U14.8 (+)
- new net P+_S-: R_sense3.2, U14.1 (-)
- new net V_P: C18.2, Q10.1 (S), R26.1, R_sense3.1, U7.6 (ANODE)
- no-connect marks 1 -> 2
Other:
- moved on the sheet: C1, C10, C11, C12, C13, C14, C15, C16, C17, C18, C19, C2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
